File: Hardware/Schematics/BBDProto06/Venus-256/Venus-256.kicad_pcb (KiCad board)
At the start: 4 copper layers, 172.7 x 109.2 mm, 231 parts, among them J201 RaspberryPi header, J301 ARM JTAG, U1001 AD7616, U101 TPS22993, U401 AD7616, U501 ATSAME70Q21A-AN, U601 AD7616, U701 AD7616, U801 AD7616, U901 ATSAME70Q21A-AN

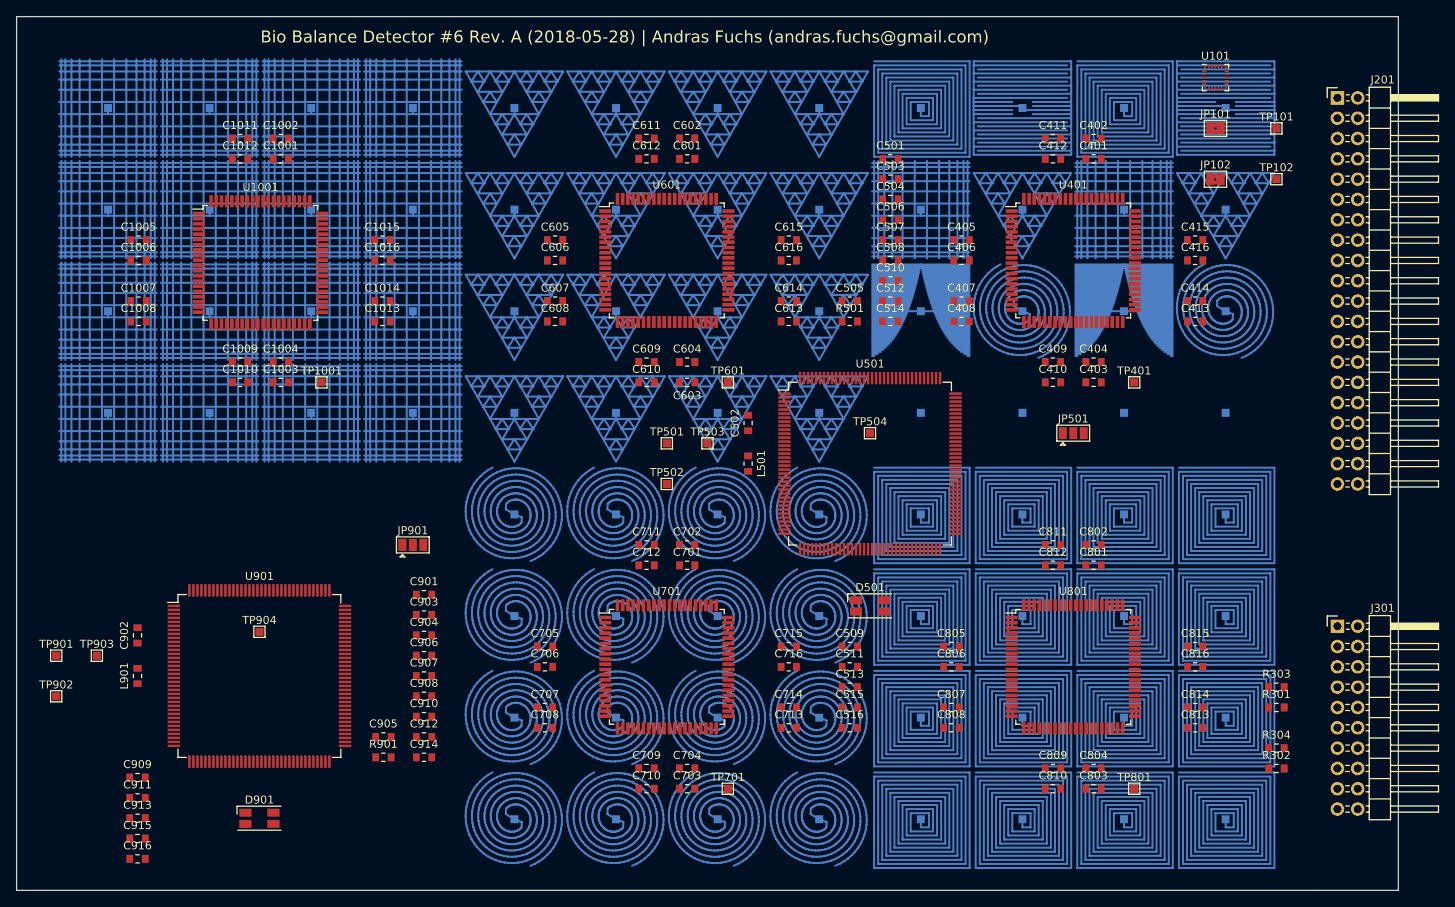
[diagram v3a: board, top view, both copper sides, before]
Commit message: Added the big pads behind the sensors
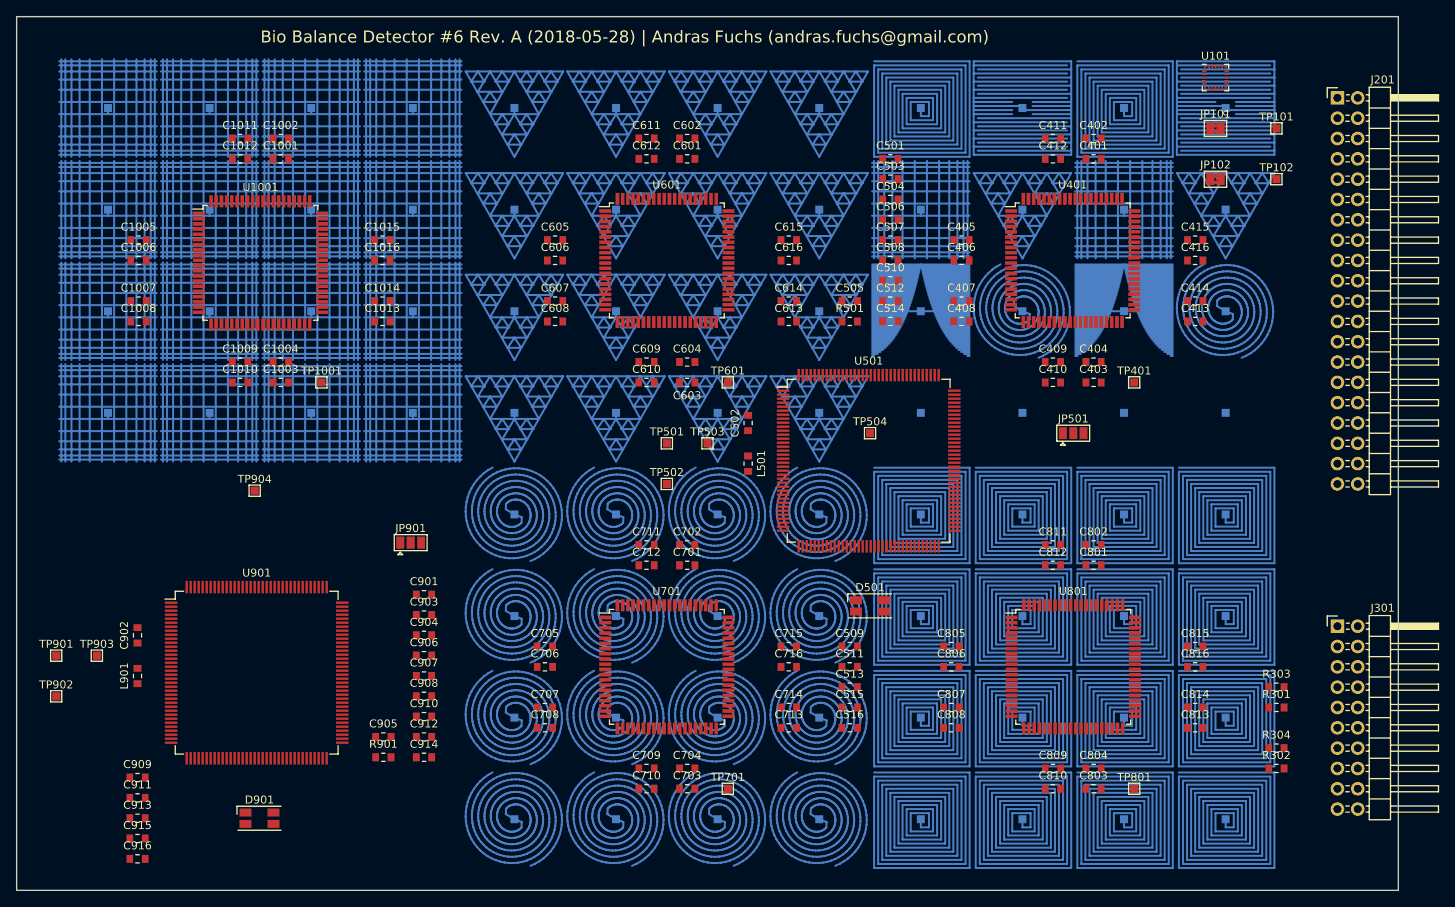
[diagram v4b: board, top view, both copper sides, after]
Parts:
- moved TP904 17.7 mm to (45.0, 74.5)
- moved U901 0.54 mm to (45.2, 97.2)
- moved U501 0.41 mm to (121.8, 70.8)
- moved JP901 0.39 mm to (64.5, 81.0)
- moved U401 0.07 mm to (147.2, 45.7)
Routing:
- net Net-(TP402-Pad1): track 299.2 -> 299.8 mm, vias 0 -> 1
- added copper zone on In1.Cu, net Net-(JP501-Pad2)
- added copper zone on In1.Cu, net Net-(JP901-Pad2)
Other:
- net class SensorLine: clearance 0.4 -> 0.254; trace_width 0.4 -> 0.254
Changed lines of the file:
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@@
     (thickness 1.6)
     (drawings 249)
-    (tracks 9412)
+    (tracks 9414)
     (zones 0)
     (modules 231)
@@
     (1 In1.Cu signal)
     (2 In2.Cu signal)
-    (31 B.Cu signal hide)
-    (33 F.Adhes user)
-    (35 F.Paste user)
+    (31 B.Cu signal)
+    (33 F.Adhes user hide)
+    (35 F.Paste user hide)
     (36 B.SilkS user hide)
-    (37 F.SilkS user)
-    (39 F.Mask user)
+    (37 F.SilkS user hide)
+    (39 F.Mask user hide)
     (40 Dwgs.User user)
     (41 Cmts.User user)
@@
     (45 Margin user)
     (46 B.CrtYd user hide)
-    (47 F.CrtYd user)
+    (47 F.CrtYd user hide)
     (49 F.Fab user)
   )
@@
   )
   (net_class SensorLine ""
-    (clearance 0.4)
-    (trace_width 0.4)
+    (clearance 0.254)
+    (trace_width 0.254)
     (via_dia 0.6)
     (via_drill 0.4)
@@
   )
   (module Package_QFP:LQFP-80_14x14mm_P0.65mm (layer F.Cu)
-    (at 147.32 45.72)
+    (at 147.25 45.72)
     (descr "80-Lead Quad Flatpack, 14x14x1.6mm Body (http://www.analog.com/media/en/technical-documentation/data-sheets/AD9852.pdf)")
     (tags "QFP 0.65")
@@
     )
   )
-  (module Package_QFP:LQFP-144_20x20mm_P0.5mm locked (layer F.Cu)
-    (at 121.92 71.12)
+  (module Package_QFP:LQFP-144_20x20mm_P0.5mm (layer F.Cu)
+    (at 121.75 70.75)
     (descr "144-Lead Plastic Low Profile Quad Flatpack (PL) - 20x20x1.40 mm Body [LQFP], 2.00 mm Footprint (see Microchip Packaging Specification 00000049BS.pdf)")
     (tags "QFP 0.5")
@@
   )
   (module Package_QFP:LQFP-144_20x20mm_P0.5mm (layer F.Cu)
-    (at 45.593 97.663)
+    (at 45.25 97.25)
     (descr "144-Lead Plastic Low Profile Quad Flatpack (PL) - 20x20x1.40 mm Body [LQFP], 2.00 mm Footprint (see Microchip Packaging Specification 00000049BS.pdf)")
     (tags "QFP 0.5")
@@
   )
   (module Jumper:SolderJumper-3_P1.3mm_Open_Pad1.0x1.5mm (layer F.Cu)
-    (at 64.77 81.28)
+    (at 64.5 81)
     (descr "SMD Solder 3-pad Jumper, 1x1.5mm Pads, 0.3mm gap, open")
     (tags "solder jumper open")
@@
   )
   (module TestPoint:TestPoint_Pad_1.0x1.0mm (layer F.Cu)
-    (at 45.595524 92.1405)
+    (at 45 74.5)
     (descr "SMD rectangular pad as test Point, square 1.0mm side length")
     (tags "test point SMD pad rectangle square")
@@
   (segment (start 172.466 26.924) (end 166.37 26.924) (width 0.254) (layer B.Cu) (net 42))
   (segment (start 160.274 26.416) (end 166.37 26.416) (width 0.254) (layer B.Cu) (net 42))
+  (segment (start 166.37 26.67) (end 166.37 27.305) (width 0.4) (layer B.Cu) (net 42))
+  (via blind (at 166.37 27.305) (size 0.6) (drill 0.4) (layers In2.Cu B.Cu) (net 42))
   (segment (start 153.67 27.686) (end 153.67 26.67) (width 0.254) (layer B.Cu) (net 43))
   (segment (start 154.686 27.686) (end 153.67 27.686) (width 0.254) (layer B.Cu) (net 43))
@@
   (segment (start 32.766 65.532) (end 26.67 65.532) (width 0.254) (layer B.Cu) (net 160))
   (segment (start 26.67 65.532) (end 20.574 65.532) (width 0.254) (layer B.Cu) (net 160))
+  (zone (net 164) (net_name "Net-(JP501-Pad2)") (layer In1.Cu) (hatch edge 0.508)
+    (connect_pads yes (clearance 0.508))
+    (min_thickness 0.254)
+    (fill yes (arc_segments 16) (thermal_gap 0.508) (thermal_bridge_width 0.508))
+    (polygon
+      (pts
+        (xy 71.25 20) (xy 173 20) (xy 173 122) (xy 71.25 122)
+      )
+    )
+  )
+  (zone (net 165) (net_name "Net-(JP901-Pad2)") (layer In1.Cu) (hatch edge 0.508)
+    (connect_pads yes (clearance 0.508))
+    (min_thickness 0.254)
+    (fill yes (arc_segments 16) (thermal_gap 0.508) (thermal_bridge_width 0.508))
+    (polygon
+      (pts
+        (xy 71 20) (xy 71 71) (xy 20 71) (xy 20 20)
+      )
+    )
+  )
 )

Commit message: Fixed the triangle nets
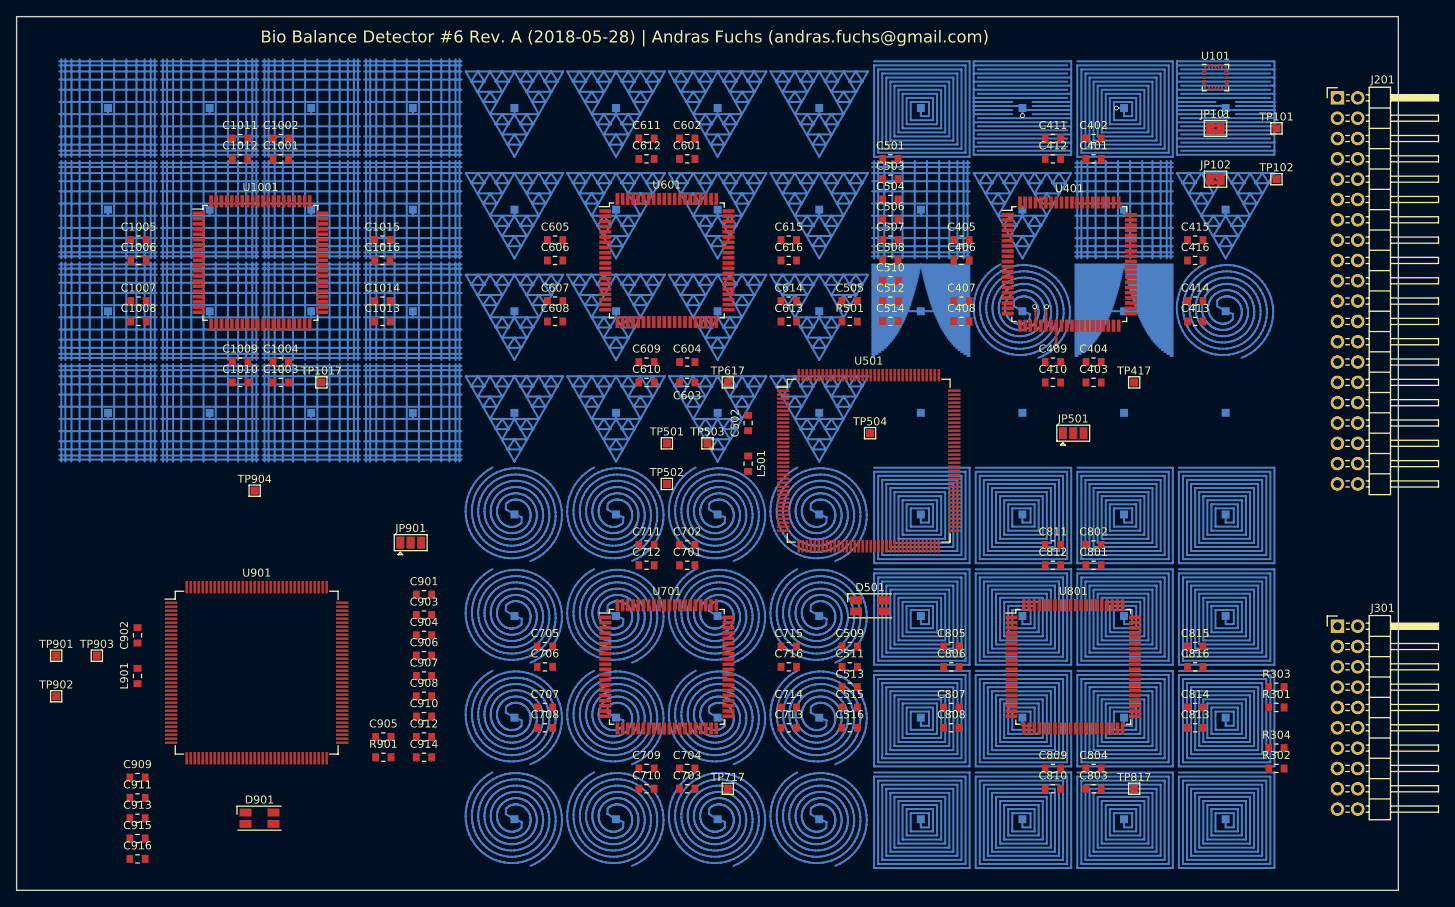
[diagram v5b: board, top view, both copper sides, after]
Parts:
- moved TP601 28.4 mm to (115.6, 26.7)
- moved TP610 28.4 mm to (102.9, 52.1)
- moved U401 0.62 mm to (146.8, 46.2)
- renumbered TP1002 to TP1001, TP1003 to TP1002, TP1004 to TP1003, TP1005 to TP1004, TP1006 to TP1005, TP1007 to TP1006, TP1008 to TP1007, TP1009 to TP1008, TP1010 to TP1009, TP1011 to TP1010, TP1012 to TP1011, TP1013 to TP1012, TP1014 to TP1013, TP1015 to TP1014, TP1016 to TP1015, TP1017 to TP1016, TP1001 to TP1017, TP402 to TP401, TP403 to TP402, TP404 to TP403, TP405 to TP404, TP406 to TP405, TP407 to TP406, TP408 to TP407, TP409 to TP408, TP410 to TP409, TP411 to TP410, TP412 to TP411, TP413 to TP412, TP414 to TP413, TP415 to TP414, TP416 to TP415, TP417 to TP416, TP401 to TP417, TP602 to TP601, TP603 to TP602, TP604 to TP603, TP605 to TP604, TP606 to TP605, TP607 to TP606, TP608 to TP607, TP609 to TP608, TP610 to TP609, TP611 to TP610, TP612 to TP611, TP613 to TP612, TP614 to TP613, TP615 to TP614, TP616 to TP615, TP617 to TP616, TP601 to TP617, TP702 to TP701, TP703 to TP702, TP704 to TP703, TP705 to TP704, TP706 to TP705, TP707 to TP706, TP708 to TP707, TP709 to TP708, TP710 to TP709, TP711 to TP710, TP712 to TP711, TP713 to TP712, TP714 to TP713, TP715 to TP714, TP716 to TP715, TP717 to TP716, TP701 to TP717, TP802 to TP801, TP803 to TP802, TP804 to TP803, TP805 to TP804, TP806 to TP805, TP807 to TP806, TP808 to TP807, TP809 to TP808, TP810 to TP809, TP811 to TP810, TP812 to TP811, TP813 to TP812, TP814 to TP813, TP815 to TP814, TP816 to TP815, TP817 to TP816, TP801 to TP817
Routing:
- net Net-(TP408-Pad1): track 13.0 -> 4780.0 mm
- net Net-(TP407-Pad1): track 4845.9 -> 125.8 mm
- net Net-(TP404-Pad1): track 1099.8 -> 300.2 mm
- net Net-(TP411-Pad1): track 525.9 -> 154.0 mm
- net Net-(TP412-Pad1): track 12.2 -> 384.1 mm
- net Net-(TP410-Pad1): track 12.2 -> 384.1 mm
- net Net-(TP409-Pad1): track 525.9 -> 154.0 mm
- net Net-(TP406-Pad1): track 60.0 -> 293.4 mm
- net Net-(TP405-Pad1): track 359.2 -> 219.9 mm
- net Net-(TP401-Pad1): track 299.8 -> 347.6 mm, vias 1 -> 2
- net Net-(TP614-Pad1): track 78.8 -> 125.8 mm
- net Net-(TP613-Pad1): track 78.8 -> 125.8 mm
- net Net-(TP610-Pad1): track 78.8 -> 125.8 mm
- net Net-(TP609-Pad1): track 78.8 -> 125.8 mm
- net Net-(TP605-Pad1): track 78.8 -> 125.8 mm
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
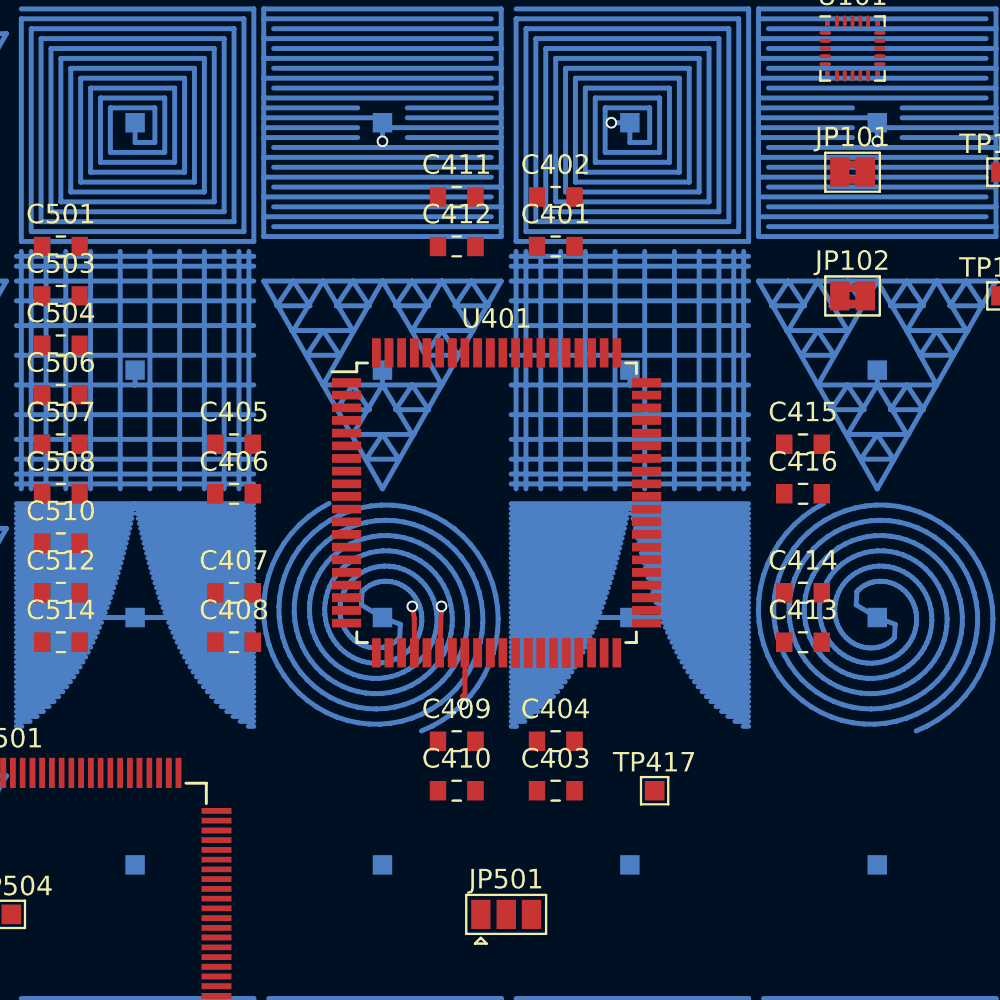
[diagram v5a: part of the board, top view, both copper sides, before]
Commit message: Added the burried vias to the first ADC
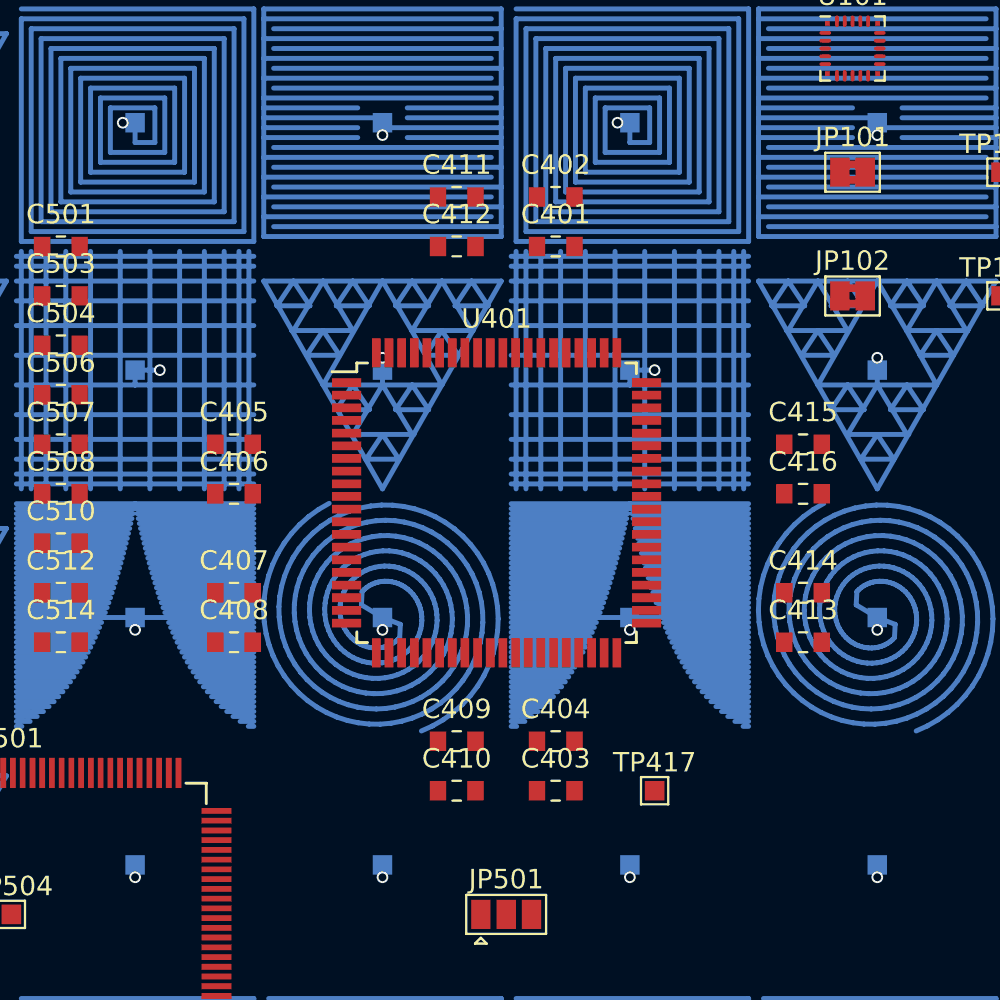
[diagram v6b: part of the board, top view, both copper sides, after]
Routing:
- net Net-(TP401-Pad1): track 347.6 -> 299.8 mm, vias 2 -> 1
- net Net-(TP402-Pad1): track 330.0 -> 300.9 mm, vias 2 -> 1
- net Net-(TP403-Pad1): track 326.5 -> 299.8 mm, vias 2 -> 1
- net Net-(TP408-Pad1): track 4780.0 -> 4781.3 mm, vias 0 -> 1
- net Net-(TP406-Pad1): track 293.4 -> 294.6 mm, vias 0 -> 1
- net Net-(TP416-Pad1): track 0.00 -> 0.64 mm, vias 0 -> 1
- net Net-(TP415-Pad1): track 0.00 -> 0.64 mm, vias 0 -> 1
- net Net-(TP414-Pad1): track 0.00 -> 0.64 mm, vias 0 -> 1
- net Net-(TP413-Pad1): track 0.00 -> 0.64 mm, vias 0 -> 1
- net Net-(TP412-Pad1): track 384.1 -> 384.7 mm, vias 0 -> 1
- net Net-(TP411-Pad1): track 154.0 -> 154.6 mm, vias 0 -> 1
- net Net-(TP410-Pad1): track 384.1 -> 384.7 mm, vias 0 -> 1
- net Net-(TP409-Pad1): track 154.0 -> 154.6 mm, vias 0 -> 1
- net Net-(TP407-Pad1): track 125.8 -> 126.5 mm, vias 0 -> 1
- net Net-(TP405-Pad1): track 219.9 -> 220.5 mm, vias 0 -> 1
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
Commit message: Switched around the ADC channels to make the PCB simpler
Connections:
- U1001 pad 12: Net-(TP1008-Pad1) -> Net-(TP1012-Pad1)
- U1001 pad 14: Net-(TP1007-Pad1) -> Net-(TP1011-Pad1)
- U1001 pad 17: Net-(TP1006-Pad1) -> Net-(TP1010-Pad1)
- U1001 pad 19: Net-(TP1005-Pad1) -> Net-(TP1009-Pad1)
- U1001 pad 2: Net-(TP1013-Pad1) -> Net-(TP1008-Pad1)
- U1001 pad 22: Net-(TP1004-Pad1) -> Net-(TP1016-Pad1)
- U1001 pad 24: Net-(TP1003-Pad1) -> Net-(TP1015-Pad1)
- U1001 pad 26: Net-(TP1002-Pad1) -> Net-(TP1014-Pad1)
- U1001 pad 28: Net-(TP1001-Pad1) -> Net-(TP1013-Pad1)
- U1001 pad 4: Net-(TP1014-Pad1) -> Net-(TP1007-Pad1)
- U1001 pad 7: Net-(TP1015-Pad1) -> Net-(TP1006-Pad1)
- U1001 pad 73: Net-(TP1009-Pad1) -> Net-(TP1001-Pad1)
- U1001 pad 75: Net-(TP1010-Pad1) -> Net-(TP1002-Pad1)
- U1001 pad 77: Net-(TP1011-Pad1) -> Net-(TP1003-Pad1)
- U1001 pad 79: Net-(TP1012-Pad1) -> Net-(TP1004-Pad1)
- U1001 pad 9: Net-(TP1016-Pad1) -> Net-(TP1005-Pad1)
- U401 pad 12: Net-(TP408-Pad1) -> Net-(TP412-Pad1)
- U401 pad 14: Net-(TP407-Pad1) -> Net-(TP411-Pad1)
- U401 pad 17: Net-(TP406-Pad1) -> Net-(TP410-Pad1)
- U401 pad 19: Net-(TP405-Pad1) -> Net-(TP409-Pad1)
- U401 pad 2: Net-(TP413-Pad1) -> Net-(TP408-Pad1)
- U401 pad 22: Net-(TP404-Pad1) -> Net-(TP416-Pad1)
- U401 pad 24: Net-(TP403-Pad1) -> Net-(TP415-Pad1)
- U401 pad 26: Net-(TP402-Pad1) -> Net-(TP414-Pad1)
- U401 pad 28: Net-(TP401-Pad1) -> Net-(TP413-Pad1)
- U401 pad 4: Net-(TP414-Pad1) -> Net-(TP407-Pad1)
- U401 pad 7: Net-(TP415-Pad1) -> Net-(TP406-Pad1)
- U401 pad 73: Net-(TP409-Pad1) -> Net-(TP401-Pad1)
- U401 pad 75: Net-(TP410-Pad1) -> Net-(TP402-Pad1)
- U401 pad 77: Net-(TP411-Pad1) -> Net-(TP403-Pad1)
- U401 pad 79: Net-(TP412-Pad1) -> Net-(TP404-Pad1)
- U401 pad 9: Net-(TP416-Pad1) -> Net-(TP405-Pad1)
- U601 pad 12: Net-(TP608-Pad1) -> Net-(TP612-Pad1)
- U601 pad 14: Net-(TP607-Pad1) -> Net-(TP611-Pad1)
- U601 pad 17: Net-(TP606-Pad1) -> Net-(TP610-Pad1)
- U601 pad 19: Net-(TP605-Pad1) -> Net-(TP609-Pad1)
- U601 pad 2: Net-(TP613-Pad1) -> Net-(TP608-Pad1)
- U601 pad 22: Net-(TP604-Pad1) -> Net-(TP616-Pad1)
- U601 pad 24: Net-(TP603-Pad1) -> Net-(TP615-Pad1)
- U601 pad 26: Net-(TP602-Pad1) -> Net-(TP614-Pad1)
- U601 pad 28: Net-(TP601-Pad1) -> Net-(TP613-Pad1)
- U601 pad 4: Net-(TP614-Pad1) -> Net-(TP607-Pad1)
- U601 pad 7: Net-(TP615-Pad1) -> Net-(TP606-Pad1)
- U601 pad 73: Net-(TP609-Pad1) -> Net-(TP601-Pad1)
- U601 pad 75: Net-(TP610-Pad1) -> Net-(TP602-Pad1)
- U601 pad 77: Net-(TP611-Pad1) -> Net-(TP603-Pad1)
- U601 pad 79: Net-(TP612-Pad1) -> Net-(TP604-Pad1)
- U601 pad 9: Net-(TP616-Pad1) -> Net-(TP605-Pad1)
- U701 pad 12: Net-(TP708-Pad1) -> Net-(TP712-Pad1)
- U701 pad 14: Net-(TP707-Pad1) -> Net-(TP711-Pad1)
- U701 pad 17: Net-(TP706-Pad1) -> Net-(TP710-Pad1)
- U701 pad 19: Net-(TP705-Pad1) -> Net-(TP709-Pad1)
- U701 pad 2: Net-(TP713-Pad1) -> Net-(TP708-Pad1)
- U701 pad 22: Net-(TP704-Pad1) -> Net-(TP716-Pad1)
- U701 pad 24: Net-(TP703-Pad1) -> Net-(TP715-Pad1)
- U701 pad 26: Net-(TP702-Pad1) -> Net-(TP714-Pad1)
- U701 pad 28: Net-(TP701-Pad1) -> Net-(TP713-Pad1)
- U701 pad 4: Net-(TP714-Pad1) -> Net-(TP707-Pad1)
- U701 pad 7: Net-(TP715-Pad1) -> Net-(TP706-Pad1)
- U701 pad 73: Net-(TP709-Pad1) -> Net-(TP701-Pad1)
- U701 pad 75: Net-(TP710-Pad1) -> Net-(TP702-Pad1)
- U701 pad 77: Net-(TP711-Pad1) -> Net-(TP703-Pad1)
- U701 pad 79: Net-(TP712-Pad1) -> Net-(TP704-Pad1)
- U701 pad 9: Net-(TP716-Pad1) -> Net-(TP705-Pad1)
- U801 pad 12: Net-(TP808-Pad1) -> Net-(TP812-Pad1)
- U801 pad 14: Net-(TP807-Pad1) -> Net-(TP811-Pad1)
- U801 pad 17: Net-(TP806-Pad1) -> Net-(TP810-Pad1)
- U801 pad 19: Net-(TP805-Pad1) -> Net-(TP809-Pad1)
- U801 pad 2: Net-(TP813-Pad1) -> Net-(TP808-Pad1)
- U801 pad 22: Net-(TP804-Pad1) -> Net-(TP816-Pad1)
- U801 pad 24: Net-(TP803-Pad1) -> Net-(TP815-Pad1)
- U801 pad 26: Net-(TP802-Pad1) -> Net-(TP814-Pad1)
- U801 pad 28: Net-(TP801-Pad1) -> Net-(TP813-Pad1)
- U801 pad 4: Net-(TP814-Pad1) -> Net-(TP807-Pad1)
- U801 pad 7: Net-(TP815-Pad1) -> Net-(TP806-Pad1)
- U801 pad 73: Net-(TP809-Pad1) -> Net-(TP801-Pad1)
- U801 pad 75: Net-(TP810-Pad1) -> Net-(TP802-Pad1)
- U801 pad 77: Net-(TP811-Pad1) -> Net-(TP803-Pad1)
- U801 pad 79: Net-(TP812-Pad1) -> Net-(TP804-Pad1)
- U801 pad 9: Net-(TP816-Pad1) -> Net-(TP805-Pad1)
